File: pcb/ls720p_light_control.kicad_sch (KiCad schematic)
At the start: 21 parts, among them J1 PWR, J2 AVRISP MK2, J3 LED_CONN, Q1 G35N02K, U1 ATTINY5, U2 SLHT50H

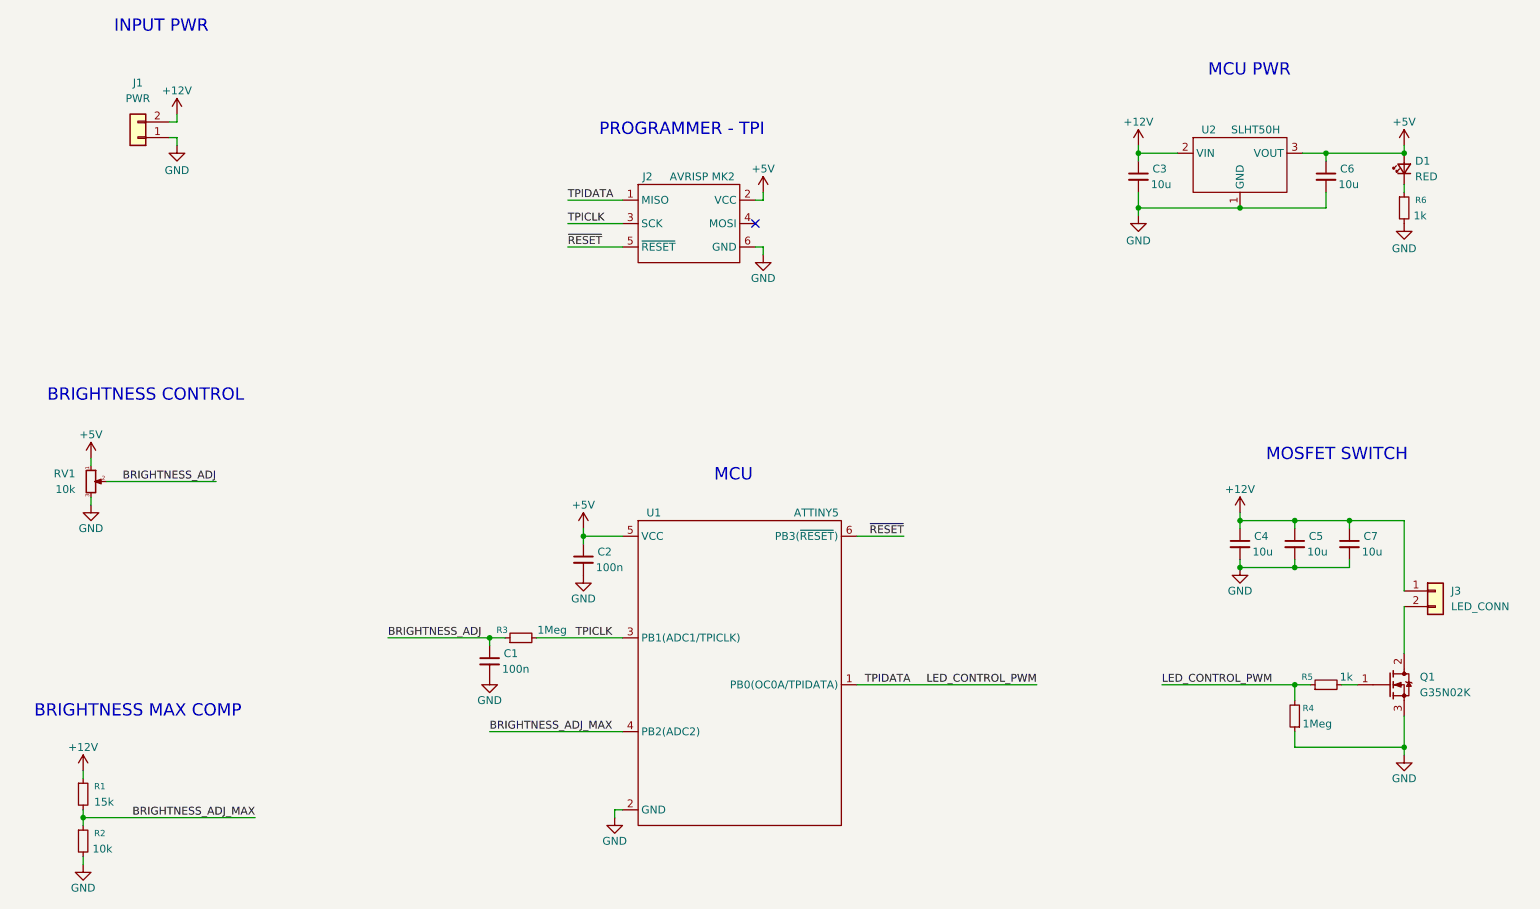
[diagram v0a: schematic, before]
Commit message: added ALT parts for LDO, MOSFET, MCU
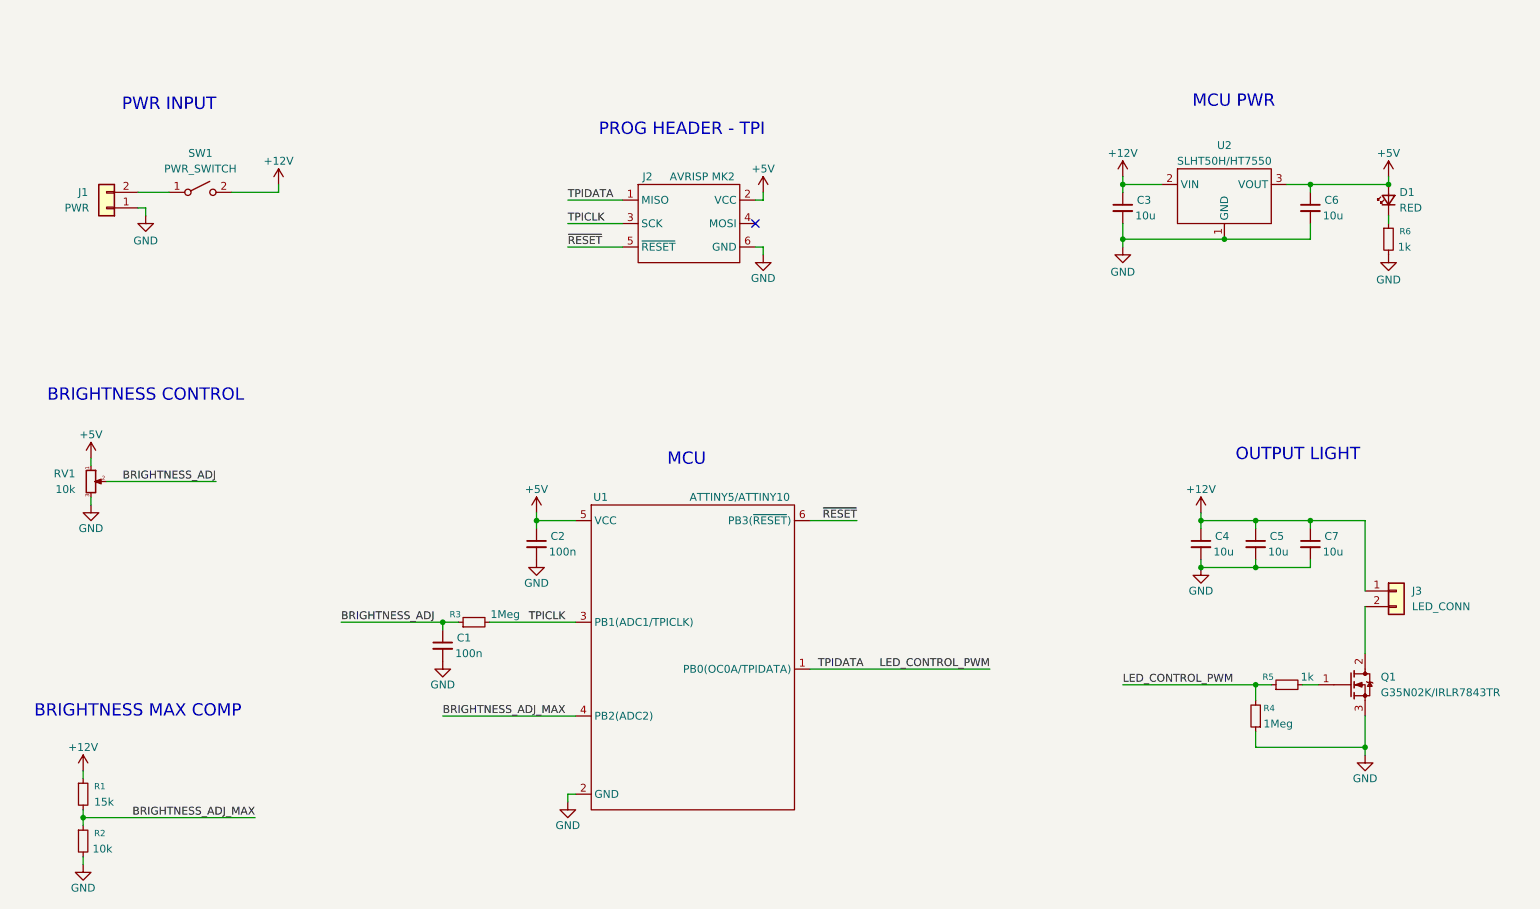
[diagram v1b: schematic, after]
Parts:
- removed RV1: 10k, symbol ls720p_light_control:PTN16-F10115K1B1
- added RV1: 10k, Connector_PinHeader_2.54mm:PinHeader_1x03_P2.54mm_Vertical, symbol Device:R_Potentiometer_Small
- added SW1: PWR_SWITCH, Connector_PinHeader_2.54mm:PinHeader_1x02_P2.54mm_Vertical, symbol Switch:SW_SPST
- Q1: value G35N02K -> G35N02K/IRLR7843TR; ALT_Datasheet (none) -> https://www.lcsc.com/datasheet/C7499399.pdf?spm=wm.sxq.inf.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; ALT_Part (none) -> IRLR7843TR; Part (none) -> G35N02K
- U1: value ATTINY5 -> ATTINY5/ATTINY10; ALT_Part (none) -> ATTINY10; Part (none) -> ATTINY5
- U2: value SLHT50H -> SLHT50H/HT7550; ALT_Datasheet (none) -> https://www.lcsc.com/datasheet/C5279053.pdf?spm=wm.sxq.inf.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; ALT_Part (none) -> TWGMC HT7550; Part (none) -> SLHT50H
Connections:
- net +12V: now also SW1.2 (B); no longer J1.2 (Pin_2)
- net +5V: now also RV1.1
- net BRIGHTNESS_ADJ: now also RV1.2
- net GND: now also RV1.3
- new net: J1.2 (Pin_2), SW1.1 (A)
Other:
- note added: "OUTPUT LIGHT"
- note added: "PROG HEADER - TPI"
- note added: "PWR INPUT"
- note removed: "INPUT PWR"
- note removed: "MOSFET SWITCH"
- note removed: "PROGRAMMER - TPI"
- moved on the sheet: C1, C2, C3, C4, C5, C6, C7, D1, J1, J3, Q1, R3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

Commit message: updated mcu info, specified package/part number
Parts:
- U1: ALT_Part ATTINY10 -> ATTINY10-TSHR; Part ATTINY5 -> ATTINY5-TSHR
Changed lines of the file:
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@@
 		(in_pos_files yes)
 		(dnp no)
-		(property "Reference" "#PWR019"
+		(property "Reference" "#PWR017"
 			(at 250.19 152.4 0)
 			(hide yes)
@@
 			(project "ls720p_light_control"
 				(path "/06998f3d-84f3-419d-9906-df41c631dead"
-					(reference "#PWR019")
+					(reference "#PWR017")
 					(unit 1)
 				)
@@
 		(in_pos_files yes)
 		(dnp no)
-		(property "Reference" "#PWR017"
+		(property "Reference" "#PWR018"
 			(at 254 55.88 0)
 			(hide yes)
@@
 			(project "ls720p_light_control"
 				(path "/06998f3d-84f3-419d-9906-df41c631dead"
-					(reference "#PWR017")
+					(reference "#PWR018")
 					(unit 1)
 				)
@@
 			)
 		)
-		(property "ALT_Part" "ATTINY10"
+		(property "ALT_Part" "ATTINY10-TSHR"
 			(at 124.46 105.41 0)
 			(hide yes)
@@
 			)
 		)
-		(property "Part" "ATTINY5"
+		(property "Part" "ATTINY5-TSHR"
 			(at 124.46 105.41 0)
 			(hide yes)
@@
 		(in_pos_files yes)
 		(dnp no)
-		(property "Reference" "#PWR018"
+		(property "Reference" "#PWR019"
 			(at 254 71.12 0)
 			(hide yes)
@@
 			(project "ls720p_light_control"
 				(path "/06998f3d-84f3-419d-9906-df41c631dead"
-					(reference "#PWR018")
-					(unit 1)
-				)
+					(reference "#PWR019")
+					(unit 1)
+				)
